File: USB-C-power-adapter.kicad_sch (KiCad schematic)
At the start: 68 parts, among them J1 USB-C_GCT_USB4105-GF-A, J2 JST_SH_1x4_SM04B-SRSS-TB-LF-SN, J3 Conn_Molex_NanoFit_1053131202, Q1 SQS401EN-T1_BE3, U1 TPD4E02B04DQA, U2 LT8350RV, U3 STUSB4500_QFN, U4 TPD4E02B04DQA

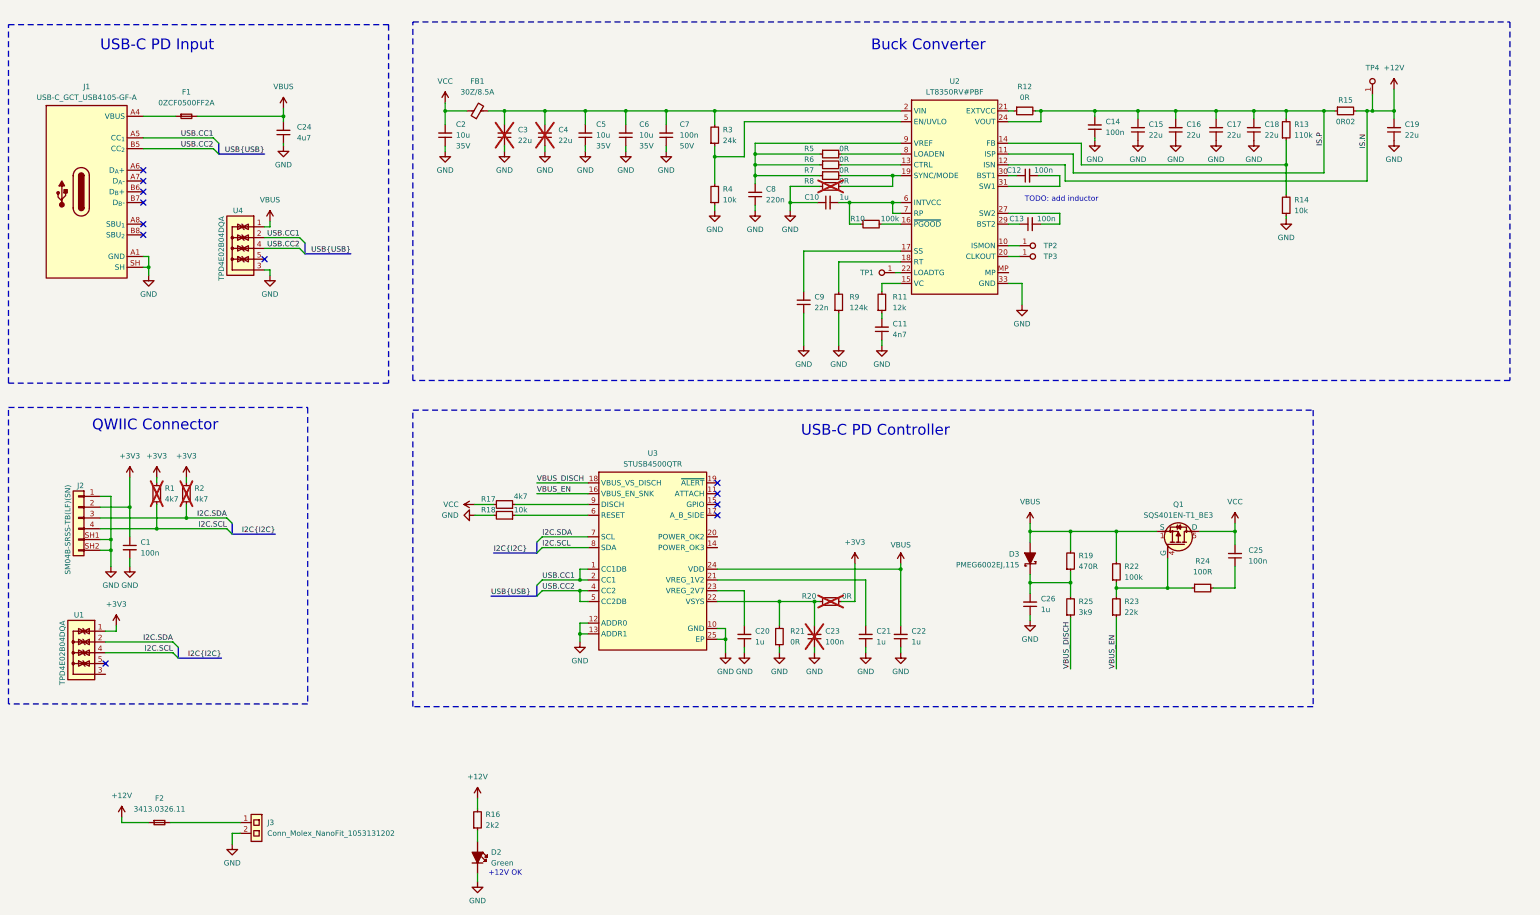
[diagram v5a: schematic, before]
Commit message: [#57006] Swap I2C lines
Align to grid
Add notes
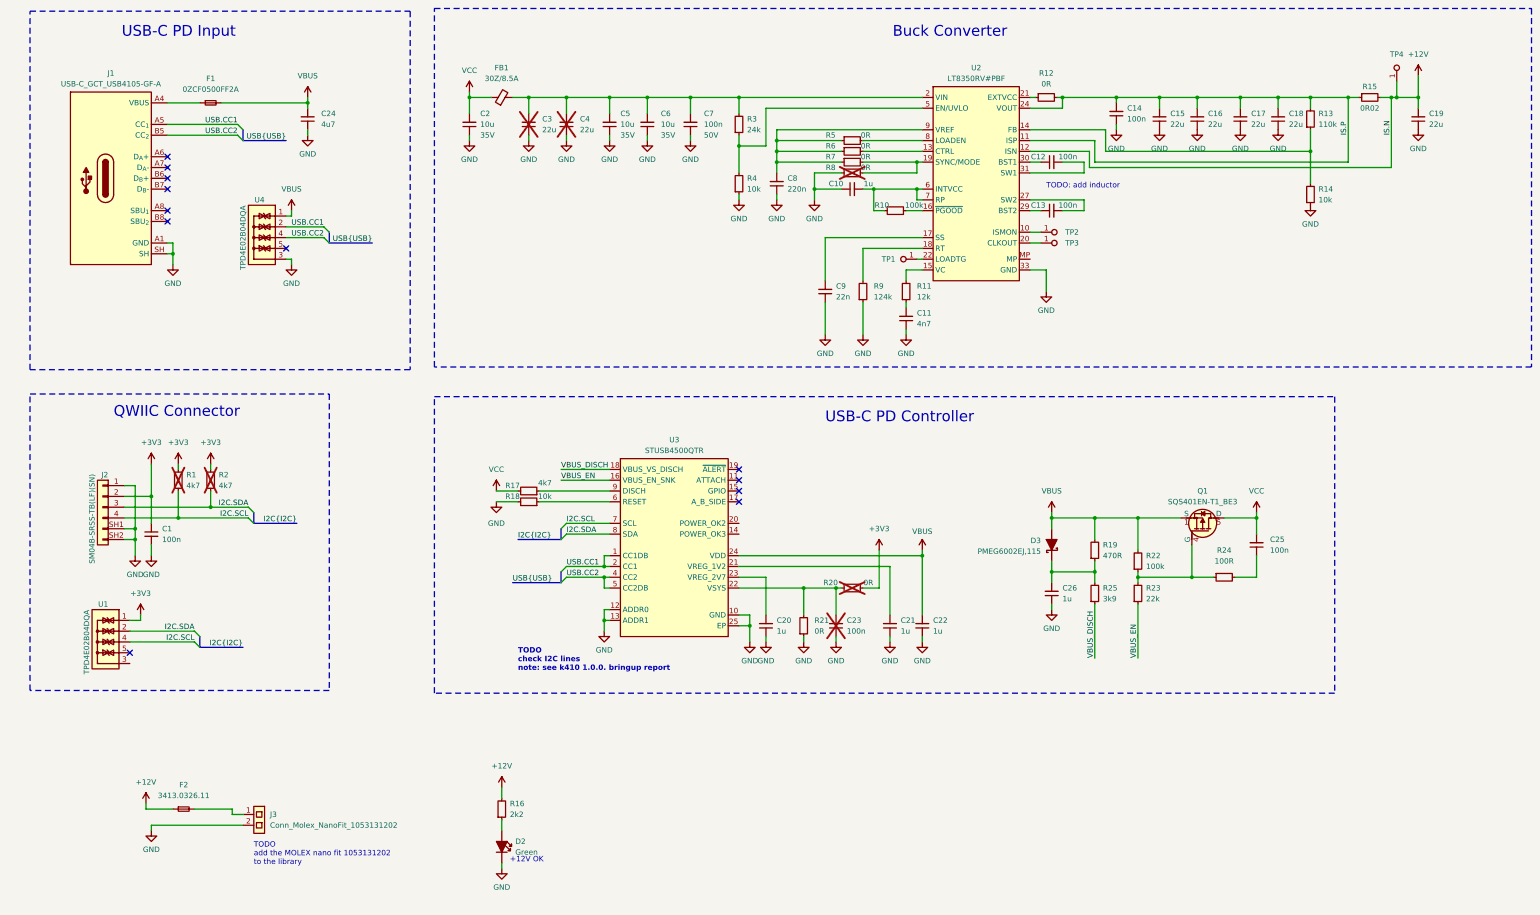
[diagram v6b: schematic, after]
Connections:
- net I2C.SCL: now also U3.7 (SCL); no longer U3.8 (SDA)
- net I2C.SDA: now also U3.8 (SDA); no longer U3.7 (SCL)
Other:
- note added: "TODO add the MOLEX nano fit 1053131202 to the library"
- note added: "TODO check I2C lines note: see k410 1.0.0. bringup report"
- moved on the sheet: C1, C10, C11, C12, C13, C14, C15, C16, C17, C18, C19, C2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

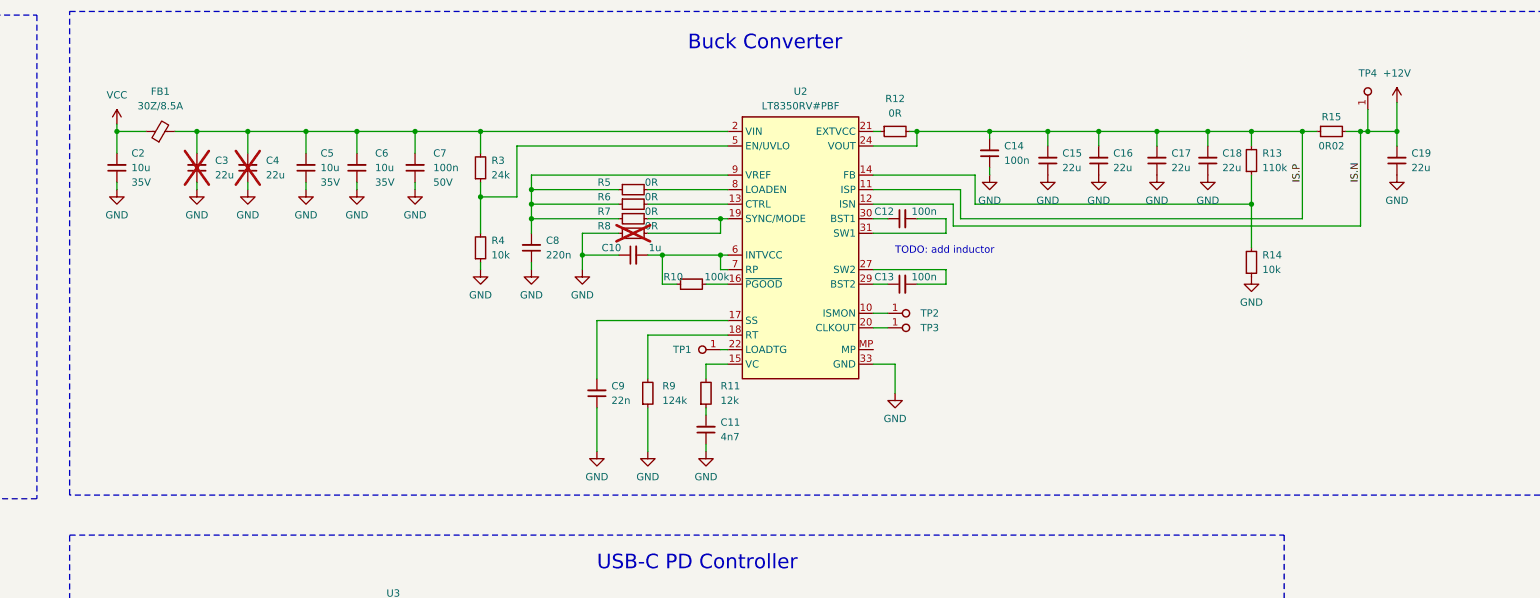
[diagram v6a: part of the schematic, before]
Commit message: [#57006] Change buck converter to SIC477ED-T1-GE3, WIP
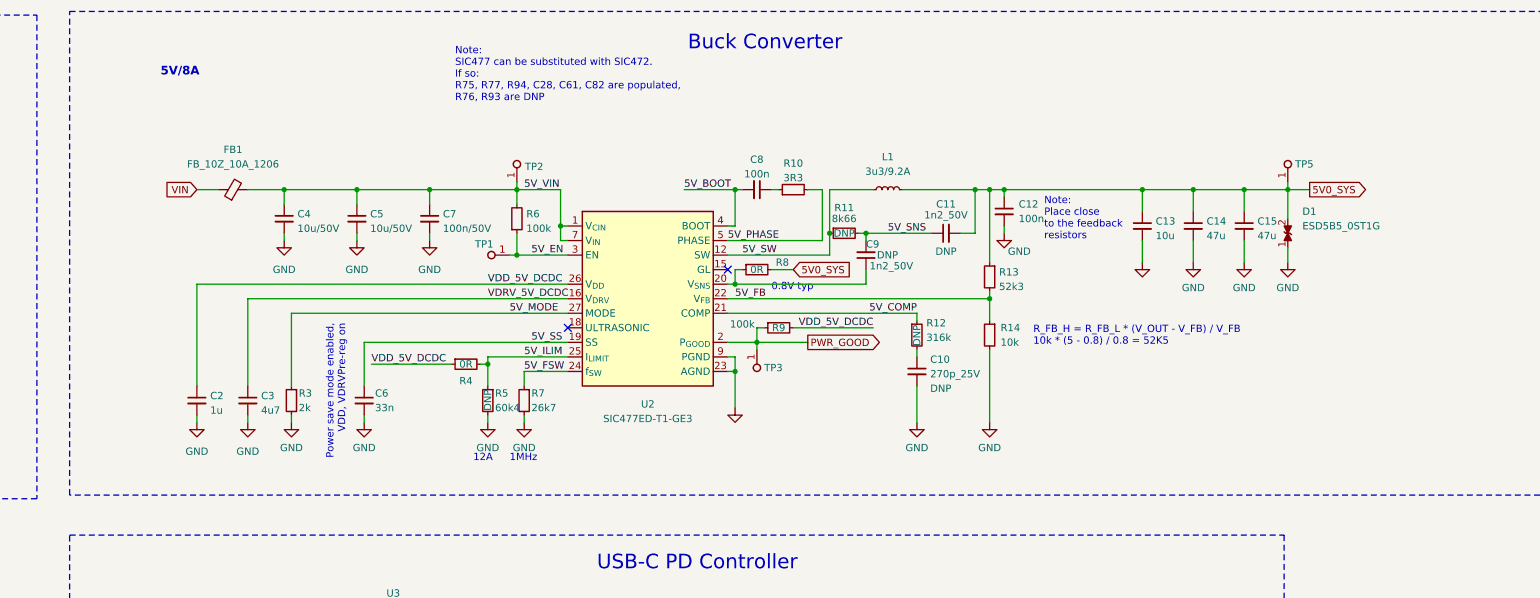
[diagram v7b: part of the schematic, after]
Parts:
- removed C10: C_1u_0402, antmicro-footprints:C_0402_1005Metric, symbol antmicroCapacitors0402:C_1u_0402
- removed C11: C_4n7_0402, antmicro-footprints:C_0402_1005Metric, symbol antmicroCapacitors0402:C_4n7_0402
- removed C13, C14: C_100n_0402, antmicro-footprints:C_0402_1005Metric, symbol antmicroCapacitors0402:C_100n_0402
- removed C15, C16, C17, C18, C19: C_22u_16V_0603, antmicro-footprints:C_0603_1608Metric, symbol antmicroCapacitors0603:C_22u_16V_0603
- removed C2, C5, C6: C_10u_0805_35V, antmicro-footprints:C_0805_2012Metric, symbol antmicroCapacitorsmisc:C_10u_0805_35V
- removed C3, C4: C_22u_1206_35V, antmicro-footprints:C_1206_3216Metric, symbol antmicroCapacitorsmisc:C_22u_1206_35V
- removed C7: C_100n_50V_X8L_0402, antmicro-footprints:C_0402_1005Metric, symbol antmicroCapacitors0402:C_100n_50V_X8L_0402
- removed C8: C_220n_6V3_X7R_0402, antmicro-footprints:C_0402_1005Metric, symbol antmicroCapacitors0402:C_220n_6V3_X7R_0402
- removed C9: C_22n_0402, antmicro-footprints:C_0402_1005Metric, symbol antmicroCapacitors0402:C_22n_0402
- removed FB1: FB_30Z_8.5A_Murata-BLM21SN_0805, antmicro-footprints:FB_0805_2012Metric, symbol antmicroFerriteBeadsandChips:FB_30Z_8.5A_Murata-BLM21SN_0805
- removed R10: R_100k_0402, antmicro-footprints:R_0402_1005Metric, symbol antmicroResistors0402:R_100k_0402
- removed R11: R_12k_0402, antmicro-footprints:R_0402_1005Metric, symbol antmicroResistors0402:R_12k_0402
- removed R12, R5, R6, R7: R_0R_0402, antmicro-footprints:R_0402_1005Metric, symbol antmicroResistors0402:R_0R_0402
- removed R13: R_110k_0402, antmicro-footprints:R_0402_1005Metric, symbol antmicroResistors0402:R_110k_0402
- removed R15: R_0R02_1206, thunderbolt-gpu-adapter-footprints:R_1206_3216Metric, symbol thunderbolt-gpu-adapter:R_0R02_1206
- removed R3: R_24k_0402, antmicro-footprints:R_0402_1005Metric, symbol antmicroResistors0402:R_24k_0402
- removed R4: R_10k_0402, antmicro-footprints:R_0402_1005Metric, symbol antmicroResistors0402:R_10k_0402
- removed R9: R_124k_0402, antmicro-footprints:R_0402_1005Metric, symbol antmicroResistors0402:R_124k_0402
- removed TP1, TP2, TP3, TP4: TP_0.75mm_SMD, antmicro-footprints:TP_SMD_0.75mm, symbol antmicroTestPoints:TP_0.75mm_SMD
- removed U2: LT8350RV, antmicro-footprints:QFN-32-4EP_4x6mm_P0.5mm, symbol antmicroDCDCConverters:LT8350RV
- added C10: C_270p_25V_0402, antmicro-footprints:C_0402_1005Metric, symbol antmicroCapacitors0402:C_270p_25V_0402
- added C11, C9: C_1n2_50V_0402, antmicro-footprints:C_0402_1005Metric, symbol antmicroCapacitors0402:C_1n2_50V_0402
- added C13: C_10u_0603, antmicro-footprints:C_0603_1608Metric, symbol antmicroCapacitors0603:C_10u_0603
- added C14, C15: C_47u_0805, antmicro-footprints:C_0805_2012Metric, symbol antmicroCapacitorsmisc:C_47u_0805
- added C2: C_1u_0402, antmicro-footprints:C_0402_1005Metric, symbol antmicroCapacitors0402:C_1u_0402
- added C3: C_4u7_0603, antmicro-footprints:C_0603_1608Metric, symbol antmicroCapacitors0603:C_4u7_0603
- added C4, C5: C_10u_1206_50V, antmicro-footprints:C_1206_3216Metric, symbol antmicroCapacitorsmisc:C_10u_1206_50V
- added C6: C_33n_0402, antmicro-footprints:C_0402_1005Metric, symbol antmicroCapacitors0402:C_33n_0402
- added C7: C_100n_50V_0402, antmicro-footprints:C_0402_1005Metric, symbol antmicroCapacitorsmisc:C_100n_50V_0402
- added C8: C_100n_0402, antmicro-footprints:C_0402_1005Metric, symbol antmicroCapacitors0402:C_100n_0402
- added D1: ESD5B5_0ST1G, antmicro-footprints:SOD-523_NP, symbol antmicroTVSDiodes:ESD5B5_0ST1G
- added FB1: FB_10Z_10A_1206, antmicro-footprints:FB_1206_3216Metric, symbol antmicroFerriteBeadsandChips:FB_10Z_10A_1206
- added L1: IHLP3232DZER3R3M01, antmicro-footprints:L_Vishay_IHLP3232DZ, symbol antmicroFixedInductors:IHLP3232DZER3R3M01
- added R10: R_3R3_0402, antmicro-footprints:R_0402_1005Metric, symbol antmicroResistors0402:R_3R3_0402
- added R11: R_8k66_0402, antmicro-footprints:R_0402_1005Metric, symbol antmicroResistors0402:R_8k66_0402
- added R12: R_316k_0402, antmicro-footprints:R_0402_1005Metric, symbol antmicroResistors0402:R_316k_0402
- added R13: R_52k3_0402, antmicro-footprints:R_0402_1005Metric, symbol antmicroResistors0402:R_52k3_0402
- added R3: R_2k_0402, antmicro-footprints:R_0402_1005Metric, symbol antmicroResistors0402:R_2k_0402
- added R4: R_0R_0402, antmicro-footprints:R_0402_1005Metric, symbol antmicroResistors0402:R_0R_0402
- added R5: R_60k4_0402, antmicro-footprints:R_0402_1005Metric, symbol antmicroResistors0402:R_60k4_0402
- added R6, R9: R_100k_0402, antmicro-footprints:R_0402_1005Metric, symbol antmicroResistors0402:R_100k_0402
- added R7: R_26k7_0402, antmicro-footprints:R_0402_1005Metric, symbol antmicroResistors0402:R_26k7_0402
- added TP1, TP2, TP3, TP5: TP_1.5mm_SMD, antmicro-footprints:TP_SMD_1.5mm, symbol antmicroTestPoints:TP_1.5mm_SMD
- added U2: SIC477ED-T1-GE3, antmicro-footprints:SIC47XED-T1-GE3, symbol antmicroDCDCConverters:SIC477ED-T1-GE3
- R8: now fitted
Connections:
- net GND: now also C12.2, R14.2, C10.2, C13.2, C14.2, C15.2, C2.2, C3.2, C4.2, C5.2, C6.2, C7.2, D1.1, R3.2, R5.2, R7.2, U2.10 (PGND), U2.11 (PGND), U2.17 (PGND), U2.23 (AGND), U2.28 (AGND), U2.9 (PGND); no longer R14.1, R8.1
- net 5V0_SYS: now reaches R8.2
- net 5V0_SYS: now also C12.1, C11.2, C13.1, C14.1, C15.1, D1.2, L1.2, R13.1, TP5.1
- new net: C8.1, R10.1
- new net: C9.1, R8.1, U2.20 (V_{SNS})
- new net: C10.1, R12.2
- new net 5V_BOOT: C8.2, U2.4 (BOOT)
- new net 5V_COMP: R12.1, U2.21 (COMP)
- new net 5V_EN: R6.1, TP1.1, U2.3 (EN)
- new net 5V_FB: R13.2, R14.1, U2.22 (V_{FB})
- new net 5V_FSW: R7.1, U2.24 (f_{SW})
- new net 5V_ILIM: R4.2, R5.1, U2.25 (I_{LIMIT})
- new net 5V_MODE: R3.1, U2.27 (MODE)
- new net 5V_PHASE: R10.2, U2.5 (PHASE), U2.6 (PHASE)
- new net 5V_SNS: C11.1, C9.2, R11.2
- new net 5V_SS: C6.1, U2.19 (SS)
- new net 5V_SW: L1.1, R11.1, U2.12 (SW), U2.13 (SW), U2.14 (SW)
- new net 5V_VIN: C4.1, C5.1, C7.1, FB1.2, R6.2, TP2.1, U2.1 (V_{CIN}), U2.7 (V_{IN}), U2.8 (V_{IN})
- new net PWR_GOOD: R9.1, TP3.1, U2.2 (P_{GOOD})
- new net VDD_5V_DCDC: C2.1, R4.1, R9.2, U2.26 (V_{DD})
- new net VDRV_5V_DCDC: C3.1, U2.16 (V_{DRV})
- new net VIN: FB1.1
- no-connect marks 12 -> 14
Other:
- note added: "0.8V typ"
- note added: "12A"
- note added: "1MHz"
- note added: "5V/8A"
- note added: "Note: Place close to the feedback resistors"
- note added: "Note: SIC477 can be substituted with SIC472. If so: R75, R77, R94, C28, C61, C82 are populated, R76, R93 are DNP"
- note added: "Power save mode enabled, VDD, VDRVPre-reg on"
- note added: "R_FB_H = R_FB_L * (V_OUT - V_FB) / V_FB 10k * (5 - 0.8) / 0.8 = 52K5"
- note removed: "TODO: add inductor"
